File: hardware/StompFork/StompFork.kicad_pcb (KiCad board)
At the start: 2 copper layers, 100.3 x 58.4 mm, 32 parts, among them J1 Line-Level Input, J2 Direct Output, J3 Stompbox Output 1, J4 Stompbox Output 2, J5 Power, U1 TL074

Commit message: Update PCB
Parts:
- moved R8 7.73 mm to (160.0, 121.9)
- moved R10 7.73 mm to (160.0, 101.6)
- moved J1 5.24 mm to (193.0, 83.8), turned to 90 degrees
- moved J4 5.20 mm to (193.0, 96.5), turned to 90 degrees
- moved C5 5.16 mm to (180.3, 116.8), turned to -90 degrees
- moved C7 5.00 mm to (180.3, 91.5), turned to -90 degrees
- moved R6 2.84 mm to (160.0, 111.8)
- moved R7 2.84 mm to (160.0, 96.5)
- moved R9 2.84 mm to (160.0, 106.7)
- moved J2 2.84 mm to (193.0, 119.4), turned to 90 degrees
- moved R5 2.84 mm to (160.0, 116.8)
- moved J3 2.80 mm to (193.0, 106.6), turned to 90 degrees
- moved RV1 2.77 mm to (109.2, 94.0), turned to -90 degrees
- moved RV2 2.70 mm to (109.2, 81.4), turned to -90 degrees
- moved J5 1.27 mm to (109.2, 119.4), turned to -90 degrees
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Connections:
- RV1 pad 1: Net-(R2-Pad1) -> VREF
- RV1 pad 3: VREF -> Net-(R2-Pad1)
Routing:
- net GND: track 270.2 -> 249.9 mm
- net VREF: track 100.2 -> 86.9 mm
- net Net-(J1-T): track 36.8 -> 33.4 mm
- net Net-(J3-T): track 22.9 -> 24.9 mm
- net Net-(R2-Pad1): track 102.8 -> 100.9 mm
- net Net-(U1C-+): track 54.0 -> 55.1 mm
- net Net-(C5-Pad1): track 11.2 -> 10.2 mm
- net Net-(R4-Pad1): track 11.2 -> 10.2 mm
- net Net-(R3-Pad1): track 11.2 -> 10.2 mm
- net Net-(U1D-+): track 53.5 -> 52.5 mm
- net Net-(C6-Pad1): track 10.2 -> 11.2 mm
- net Net-(C7-Pad1): track 11.3 -> 12.3 mm
- net Net-(J4-T): track 24.0 -> 25.0 mm
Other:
- board size 100.3 x 58.4 mm -> 100.3 x 50.8 mm

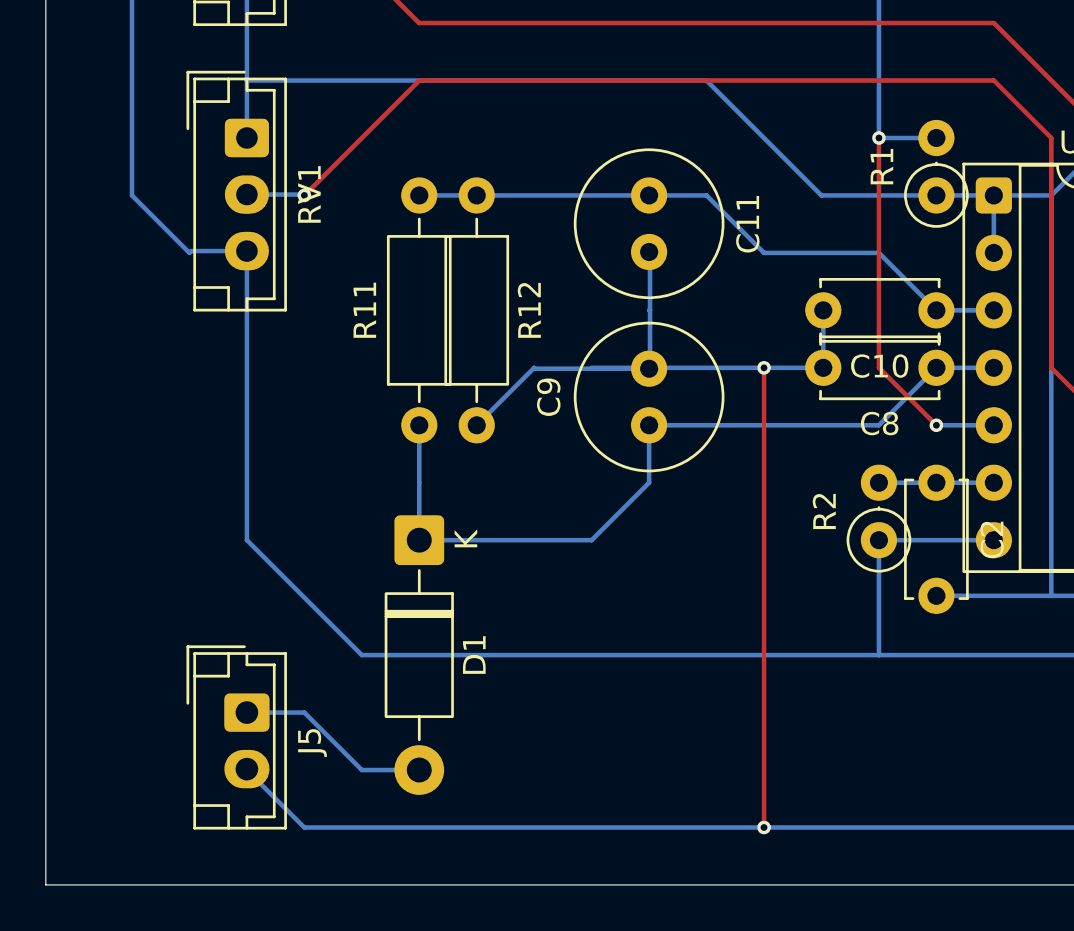
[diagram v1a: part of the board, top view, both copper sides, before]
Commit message: Add status LED
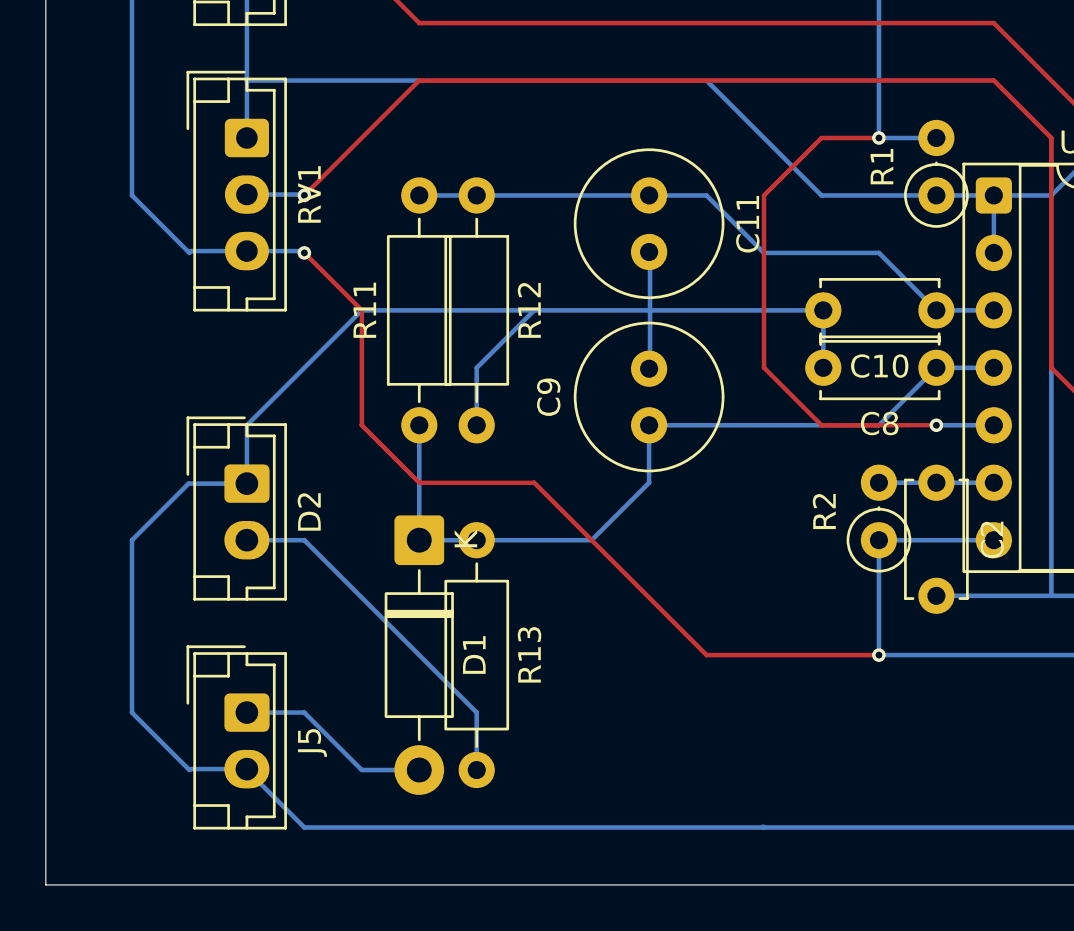
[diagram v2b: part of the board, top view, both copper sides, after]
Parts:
- added D2: LED, Connector_JST:JST_EH_B2B-EH-A_1x02_P2.50mm_Vertical, F.Cu at (109.2, 109.3)
- added R13: 3k3, Resistor_THT:R_Axial_DIN0207_L6.3mm_D2.5mm_P10.16mm_Horizontal, F.Cu at (119.4, 111.8)
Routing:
- net GND: track 249.9 -> 266.9 mm, vias 2 -> 0
- net Net-(D2-A): track 0.00 -> 15.9 mm
- net Net-(U1B-+): track 29.0 -> 37.7 mm
- net Net-(R2-Pad1): track 100.9 -> 96.4 mm, vias 0 -> 2

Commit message: Rename VREF to VGND
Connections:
- net VREF renamed VGND
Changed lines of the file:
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@@
 	(net 1 "VCC")
 	(net 2 "Net-(D1-A)")
-	(net 3 "VREF")
+	(net 3 "VGND")
 	(net 4 "Net-(U1B-+)")
 	(net 5 "GND")
@@
 			(layers "*.Cu" "*.Mask")
 			(remove_unused_layers no)
-			(net 3 "VREF")
+			(net 3 "VGND")
 			(pintype "passive")
 		)
@@
 			(layers "*.Cu" "*.Mask")
 			(remove_unused_layers no)
-			(net 3 "VREF")
+			(net 3 "VGND")
 			(pintype "passive")
 		)
@@
 			(remove_unused_layers no)
 			(roundrect_rratio 0.15625)
-			(net 3 "VREF")
+			(net 3 "VGND")
 			(pintype "output")
 		)
@@
 			(layers "*.Cu" "*.Mask")
 			(remove_unused_layers no)
-			(net 3 "VREF")
+			(net 3 "VGND")
 			(pinfunction "-")
 			(pintype "input")
@@
 			(remove_unused_layers no)
 			(roundrect_rratio 0.147059)
-			(net 3 "VREF")
+			(net 3 "VGND")
 			(pinfunction "1")
 			(pintype "passive")
@@
 			(layers "*.Cu" "*.Mask")
 			(remove_unused_layers no)
-			(net 3 "VREF")
+			(net 3 "VGND")
 			(pintype "passive")
 		)
@@
 			(layers "*.Cu" "*.Mask")
 			(remove_unused_layers no)
-			(net 3 "VREF")
+			(net 3 "VGND")
 			(pintype "passive")
 		)
@@
 			(layers "*.Cu" "*.Mask")
 			(remove_unused_layers no)
-			(net 3 "VREF")
+			(net 3 "VGND")
 			(pinfunction "3")
 			(pintype "passive")
